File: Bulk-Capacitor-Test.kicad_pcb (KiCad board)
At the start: 2 copper layers, 163 x 88 mm, 62 parts, among them J1 Conn_01x01_Socket, J2 Conn_01x01_Socket, J3 Conn_01x01_Socket, J4 Conn_01x01_Socket

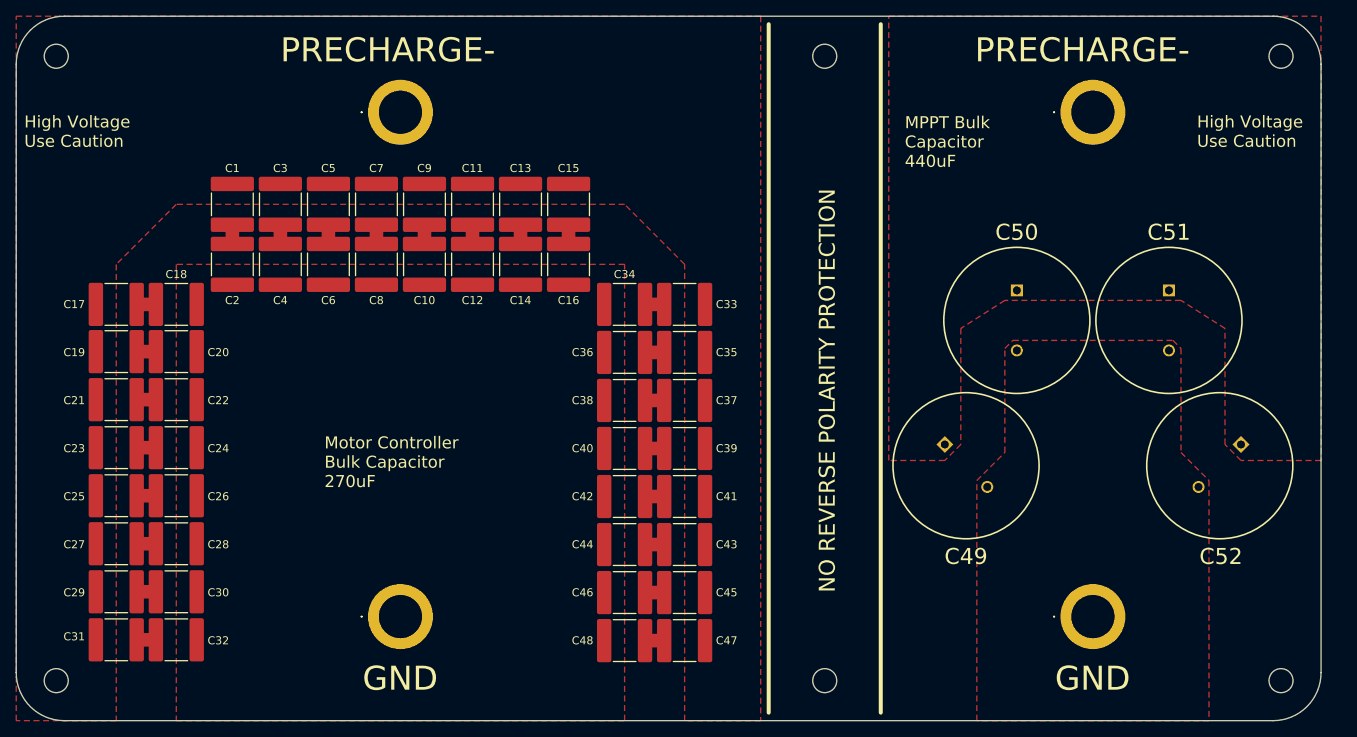
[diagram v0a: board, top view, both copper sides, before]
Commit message: added testpoints
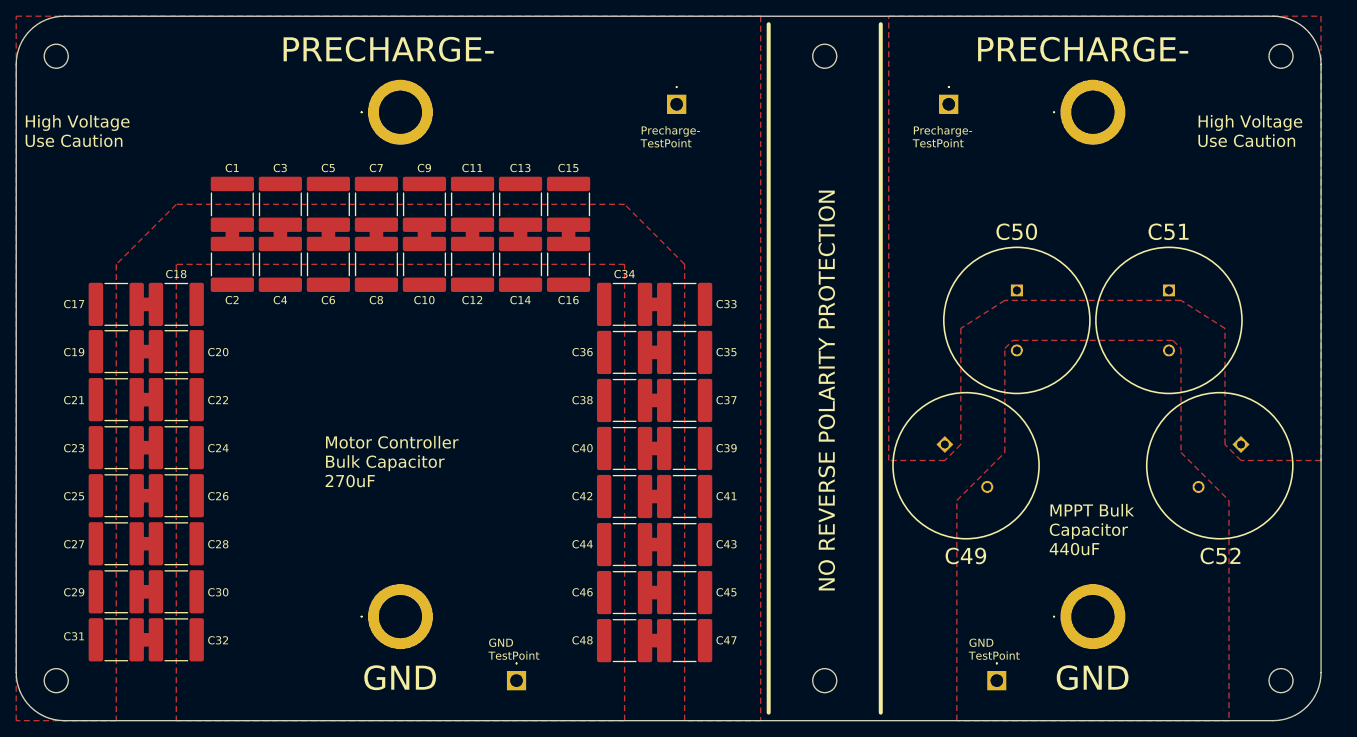
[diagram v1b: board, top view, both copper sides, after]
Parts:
- added TP1: TestPoint, BCT:5281, F.Cu at (162.5, 48.0)
- added TP2: TestPoint, BCT:5281, F.Cu at (196.5, 48.0)
- added TP3: TestPoint, BCT:5281, F.Cu at (142.5, 120.0)
- added TP4: TestPoint, BCT:5281, F.Cu at (202.5, 120.0)
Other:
- board text added: "GND TestPoint"
- board text added: "Precharge- TestPoint"

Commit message: now two boards
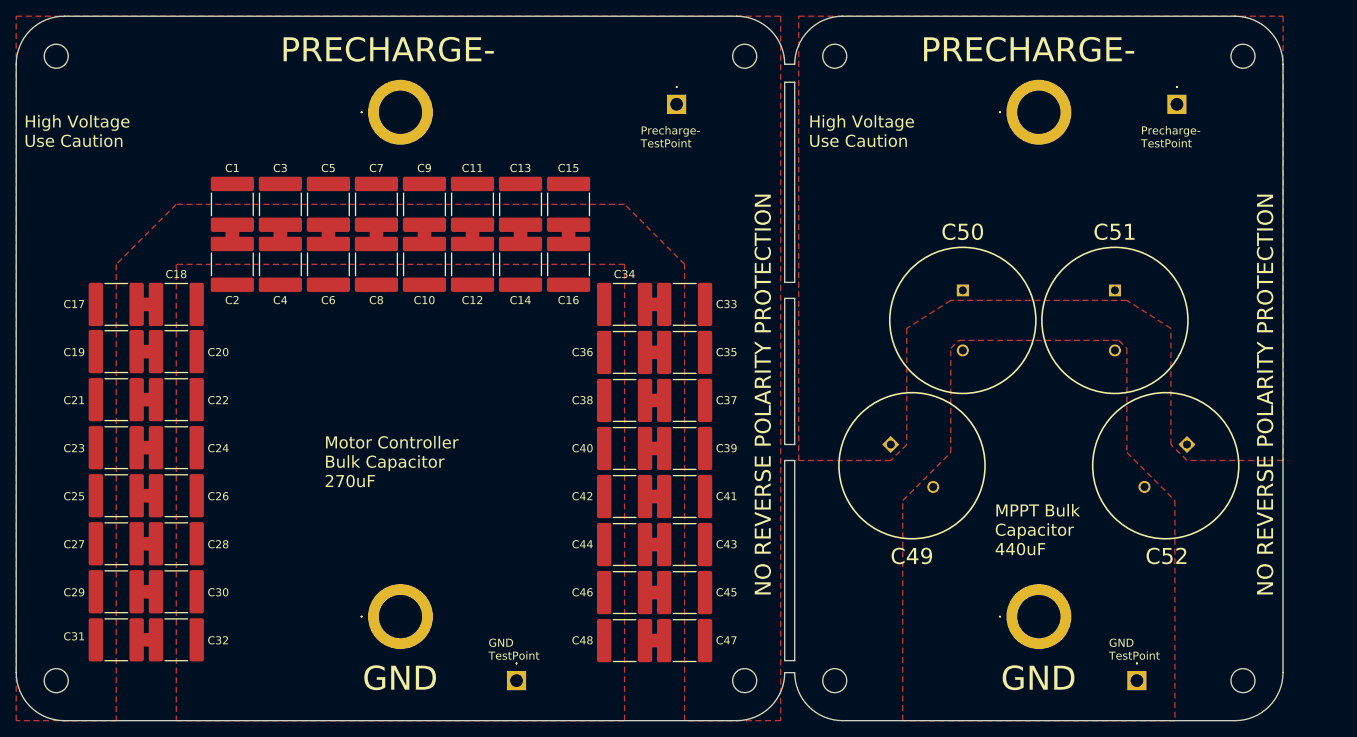
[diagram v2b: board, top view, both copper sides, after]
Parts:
- added H7: MountingHole, MountingHole:MountingHole_3mm, F.Cu at (182.2, 42.0)
- added H8: MountingHole, MountingHole:MountingHole_3mm, F.Cu at (182.2, 120.0)
- moved TP2 28.5 mm to (225.0, 48.0)
- moved TP4 17.5 mm to (220.0, 120.0)
- moved H3 10.0 mm to (171.0, 42.0)
- moved H4 10.0 mm to (171.0, 120.0)
- moved C49 6.75 mm to (226.2, 90.5)
- moved C50 6.75 mm to (217.2, 71.2)
- moved C51 6.75 mm to (198.2, 71.2)
- moved C52 6.75 mm to (189.2, 90.5)
- moved J3 6.75 mm to (207.8, 49.0)
- moved J4 6.75 mm to (207.8, 112.0)
- moved H5 4.75 mm to (233.2, 42.0)
- moved H6 4.75 mm to (233.2, 120.0)
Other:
- board size 163 x 88 mm -> 158.2 x 88 mm
